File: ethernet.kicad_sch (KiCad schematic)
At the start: 44 parts, among them U1 MPFS250T-FCVG484, U16 DP83867ISRGZR

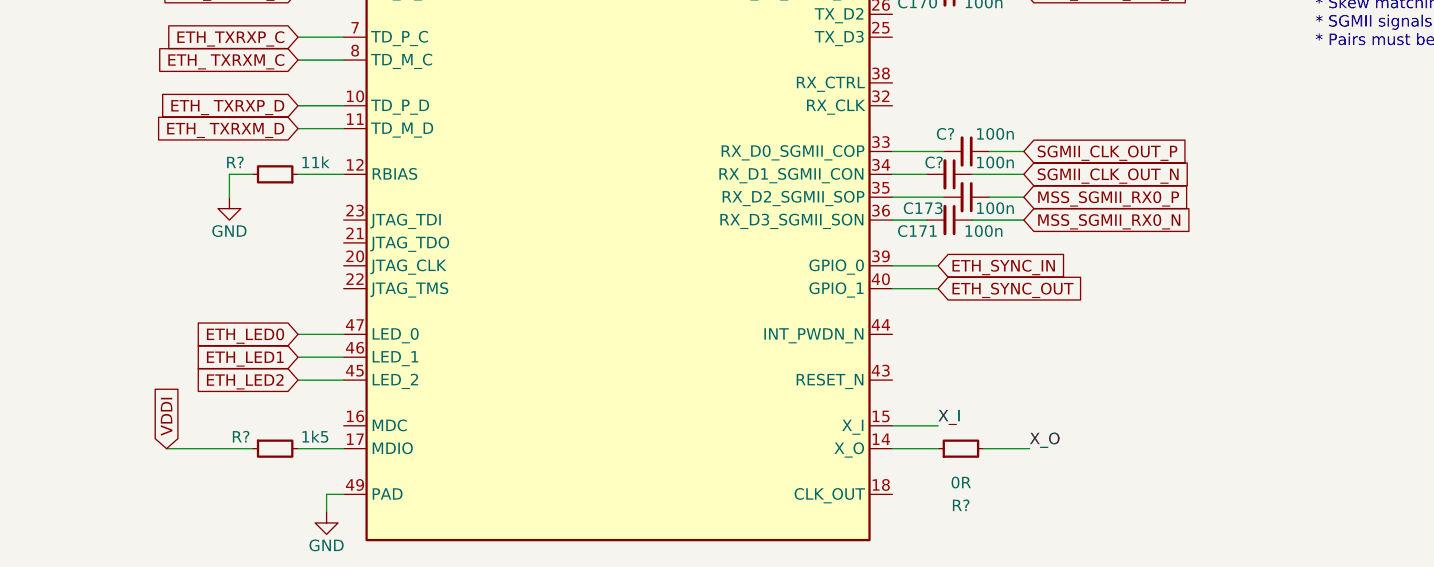
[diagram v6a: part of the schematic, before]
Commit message: [#54442] Connect reset and pwdn signals to PF
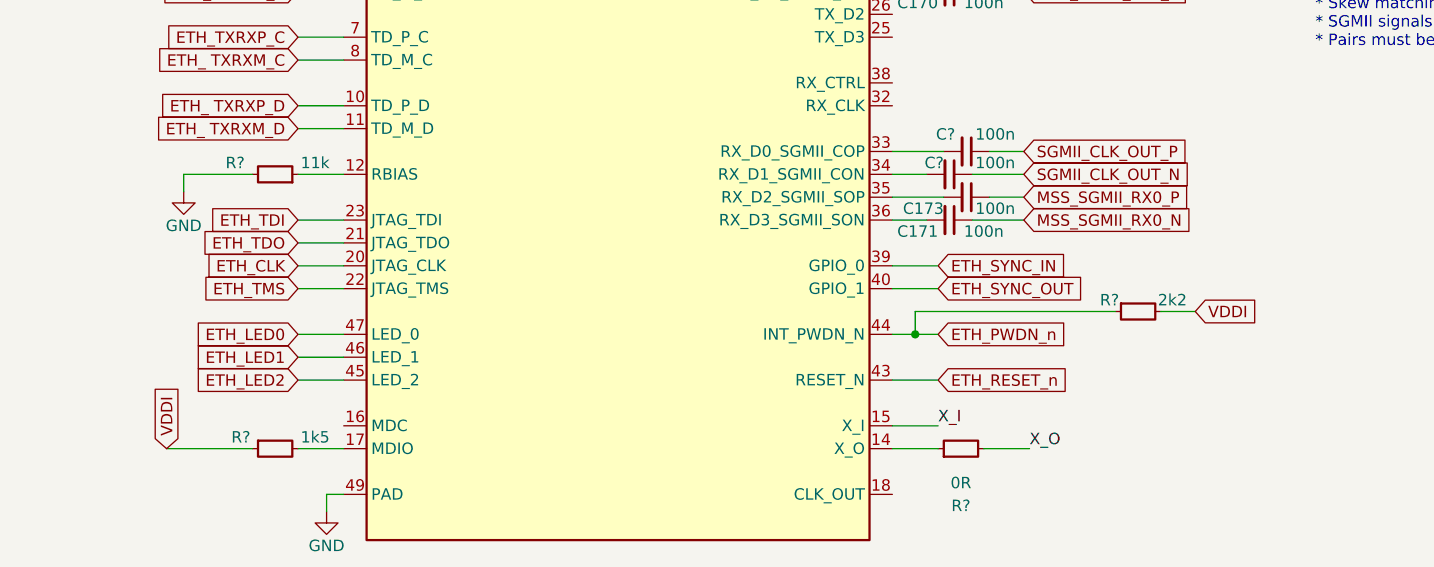
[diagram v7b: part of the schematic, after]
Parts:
- added R?: R_2k2_0402, antmicro-footprints:R_0402_1005Metric, symbol antmicroResistors0402:R_2k2_0402
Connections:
- net VDDI: now also R?.2
- net ETH_CLK: now reaches U16.20 (JTAG_CLK)
- net ETH_TDO: now reaches U16.21 (JTAG_TDO)
- net ETH_TMS: now reaches U16.22 (JTAG_TMS)
- net ETH_TDI: now reaches U16.23 (JTAG_TDI)
- net ETH_RESET_n: now reaches U16.43 (RESET_N)
- net ETH_PWDN_n: now reaches U16.44 (INT_PWDN_N)
- net ETH_PWDN_n: now also R?.1
